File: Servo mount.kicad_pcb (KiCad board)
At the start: 2 copper layers, 80 x 34.6 mm, 35 parts, among them IC1 ATTINY84-SS, K5 CONN_3, K6 CONN_3, P1 CONN_3X2, Q1 BC847, Q2 BC847, U1 UA78L05, U2 BUZ11

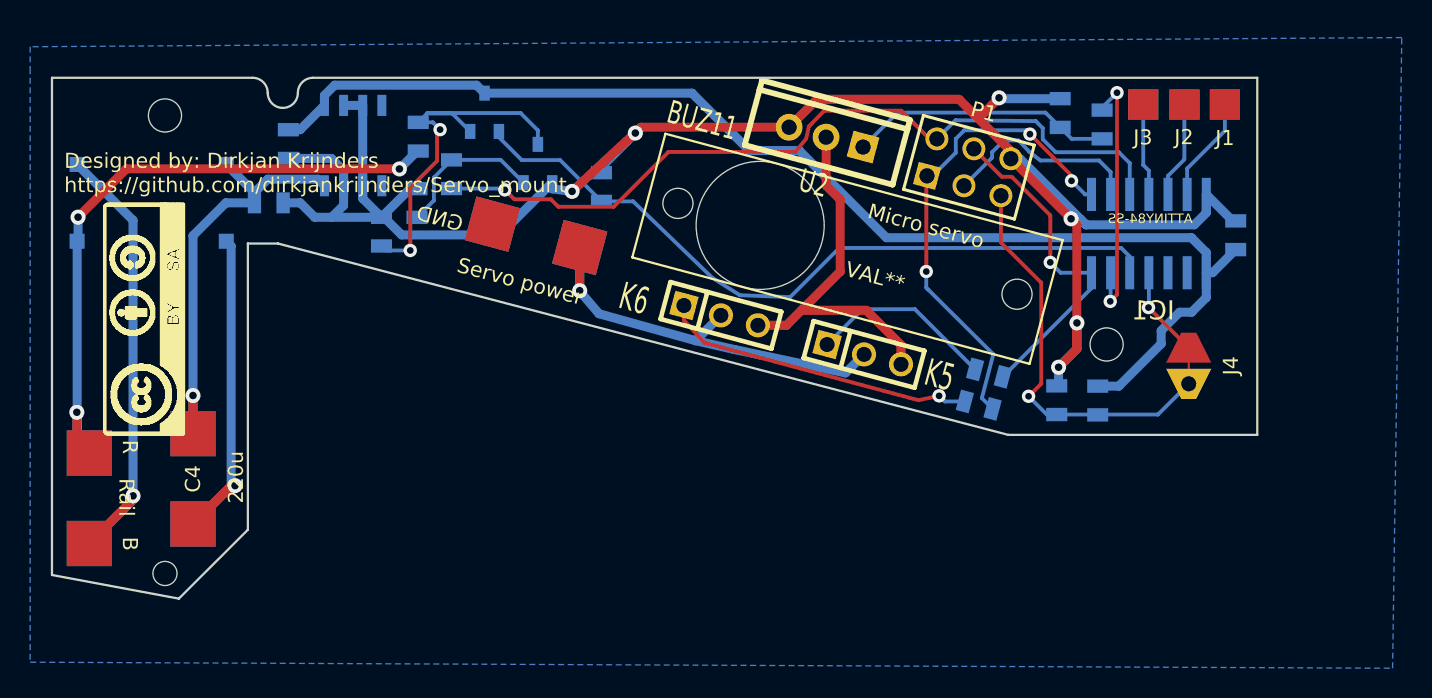
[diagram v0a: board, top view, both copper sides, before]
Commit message: Fixed rev 1 issues
- Moved all pad away from foot to allow for mounting under crossing
- Fixed the “hole” for the servo
- Fixed the order of J4 to really allow debug wire access
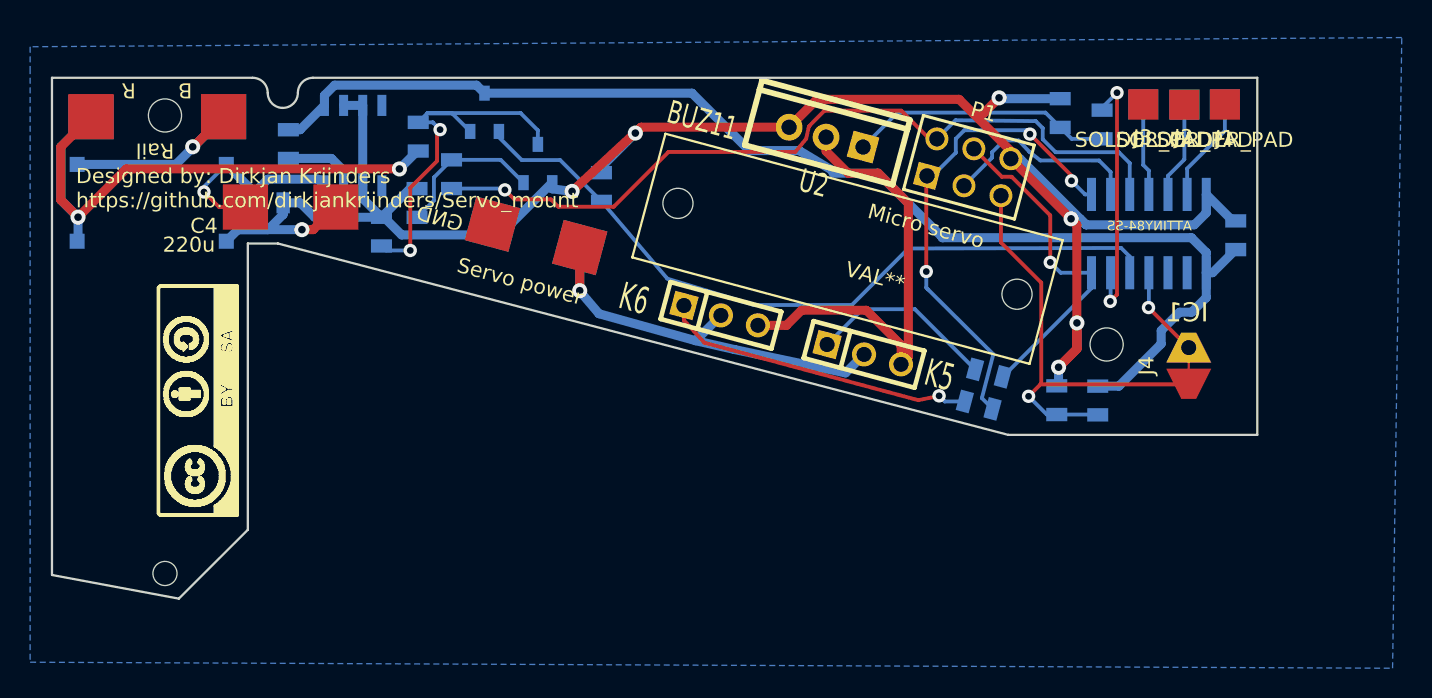
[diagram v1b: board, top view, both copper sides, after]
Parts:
- J1, J2, J3: value ~ -> SOLDER_PAD
- U1: value UA78L05 -> uA78L05
- moved ~ 25.5 mm to (105.6, 102.6), turned to 180 degrees
- moved C4 19.2 mm to (115.8, 108.6), turned to 0 degrees
- moved ? 6.48 mm to (112.3, 129.1)
- turned J4 to 90 degrees
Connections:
- IC1 pad 2: (no net) -> Net-(IC1-Pad2)
- IC1 pad 3: (no net) -> Net-(IC1-Pad3)
- IC1 pad 4: N-000009 -> Net-(IC1-Pad4)
- J4 pad 1: N-000009 -> Reset
- J4 pad 2: Reset -> Net-(IC1-Pad4)
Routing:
- net -VAA: track 32.3 -> 14.0 mm
- net Net-(C4-Pad1): track 32.4 -> 14.8 mm
- net GND: track 158.4 -> 143.2 mm
- net Net-(IC1-Pad4): track 0.00 -> 6.09 mm, vias 0 -> 1
- net N-000009: track 6.09 -> 0.00 mm, vias 1 -> 0
- net AGND: track 25.1 -> 30.9 mm
- net VAA: track 46.5 -> 42.0 mm, vias 3 -> 2
- net Reset: track 26.8 -> 29.7 mm

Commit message: Moved tracks away from servo hole
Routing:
- net AGND: track 30.9 -> 33.6 mm
- net Net-(K5-Pad1): track 12.4 -> 11.2 mm
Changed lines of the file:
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@@
     (thickness 1.6)
     (drawings 25)
-    (tracks 304)
+    (tracks 303)
     (zones 0)
     (modules 35)
@@
       (effects (font (size 1 1) (thickness 0.15)))
     )
-    (fp_circle (center -2 0) (end 0 -0.2) (layer Eco2.User) (width 2))
-    (fp_circle (center -6 0) (end -3.5 2) (layer Eco2.User) (width 2))
+    (fp_circle (center -2 0) (end 0 -0.2) (layer Edge.Cuts) (width 2))
+    (fp_circle (center -6 0) (end -3.5 2) (layer Edge.Cuts) (width 2))
     (fp_line (start 13.65 4.25) (end -13.65 4.25) (layer F.SilkS) (width 0.15))
     (fp_line (start -13.65 -4.25) (end 13.65 -4.25) (layer F.SilkS) (width 0.15))
@@
   (segment (start 108.22016 105.74984) (end 109.34 104.63) (width 0.6) (layer B.Cu) (net 2))
   (segment (start 109.34 104.63) (end 111.39 102.58) (width 0.6) (layer B.Cu) (net 2))
-  (segment (start 156.353452 119.0174) (end 156.84 118.530852) (width 0.6) (layer F.Cu) (net 3))
+  (segment (start 156.353452 119.0174) (end 160.09 115.280852) (width 0.6) (layer F.Cu) (net 3) (status 400000))
+  (segment (start 160.09 111.58) (end 154.84 106.33) (width 0.6) (layer F.Cu) (net 3))
+  (segment (start 160.09 115.280852) (end 160.09 111.58) (width 0.6) (layer F.Cu) (net 3))
+  (segment (start 154.84 106.33) (end 152.84 106.33) (width 0.6) (layer F.Cu) (net 3))
   (segment (start 151.38 104.87) (end 151.38 103.94) (width 0.6) (layer F.Cu) (net 3))
   (segment (start 152.84 106.33) (end 151.38 104.87) (width 0.6) (layer F.Cu) (net 3))
-  (segment (start 154.84 106.33) (end 152.84 106.33) (width 0.6) (layer F.Cu) (net 3))
-  (segment (start 156.84 108.33) (end 154.84 106.33) (width 0.6) (layer F.Cu) (net 3))
-  (segment (start 156.84 109.08) (end 156.84 108.33) (width 0.6) (layer F.Cu) (net 3))
-  (segment (start 156.84 118.530852) (end 156.84 109.08) (width 0.6) (layer F.Cu) (net 3))
   (segment (start 156.353452 119.0174) (end 156.353452 117.733452) (width 0.6) (layer F.Cu) (net 3))
   (segment (start 154.05 115.43) (end 149.75 115.43) (width 0.6) (layer F.Cu) (net 3))
@@
   (via (at 170.24 114.84) (size 0.889) (layers F.Cu B.Cu) (net 6))
   (segment (start 170.265 114.815) (end 170.24 114.84) (width 0.254) (layer B.Cu) (net 6))
+  (segment (start 162.34 117.58) (end 162.48 117.72) (width 0.254) (layer B.Cu) (net 7))
+  (segment (start 162.430044 121.976525) (end 161.72 121.26) (width 0.254) (layer B.Cu) (net 7))
+  (segment (start 161.72 121.26) (end 162.48 118.35) (width 0.254) (layer B.Cu) (net 7))
+  (segment (start 162.34 110.771477) (end 162.34 117.58) (width 0.254) (layer F.Cu) (net 7))
+  (via (at 162.34 117.58) (size 0.889) (layers F.Cu B.Cu) (net 7))
+  (segment (start 162.34 110.771477) (end 158.077848 106.509325) (width 0.254) (layer F.Cu) (net 7) (status 800000))
+  (segment (start 162.48 117.72) (end 162.48 118.35) (width 0.254) (layer B.Cu) (net 7))
   (segment (start 158.077848 106.509325) (end 158.450675 106.509325) (width 0.254) (layer B.Cu) (net 7))
   (via (at 167.67 106.84) (size 0.889) (layers F.Cu B.Cu) (net 7))
@@
   (segment (start 158.450675 106.509325) (end 159.99 104.97) (width 0.254) (layer B.Cu) (net 7))
   (segment (start 158.077848 106.509325) (end 158.03 106.557173) (width 0.254) (layer F.Cu) (net 7))
-  (segment (start 161.72 121.26) (end 162.48 118.35) (width 0.254) (layer B.Cu) (net 7))
-  (segment (start 162.48 118.35) (end 158.15 114.05) (width 0.254) (layer B.Cu) (net 7))
-  (segment (start 161.72 121.26) (end 162.430044 121.976525) (width 0.254) (layer B.Cu) (net 7))
-  (segment (start 158.03 113.93) (end 158.15 114.05) (width 0.254) (layer B.Cu) (net 7))
-  (segment (start 158.03 112.86) (end 158.03 113.93) (width 0.254) (layer B.Cu) (net 7))
-  (via (at 158.03 112.86) (size 0.889) (layers F.Cu B.Cu) (net 7))
-  (segment (start 158.03 106.557173) (end 158.03 112.86) (width 0.254) (layer F.Cu) (net 7))
   (segment (start 168.995 112.93842) (end 166.94842 112.93842) (width 0.254) (layer B.Cu) (net 8))
   (segment (start 163.045426 106.57) (end 161.1887 104.713274) (width 0.254) (layer F.Cu) (net 8))
@@
   (segment (start 175.44 117.91) (end 175.45 117.91) (width 0.254) (layer F.Cu) (net 16))
   (segment (start 172.78 115.25) (end 175.44 117.91) (width 0.254) (layer F.Cu) (net 16))
-  (segment (start 161.269956 119.353475) (end 157.276481 115.36) (width 0.254) (layer B.Cu) (net 17))
-  (segment (start 153.789148 115.36) (end 151.446548 117.7026) (width 0.254) (layer B.Cu) (net 17))
-  (segment (start 157.276481 115.36) (end 153.789148 115.36) (width 0.254) (layer B.Cu) (net 17))
+  (segment (start 161.269956 119.353475) (end 158.746481 116.83) (width 0.254) (layer B.Cu) (net 17) (status 400000))
+  (segment (start 152.319148 116.83) (end 151.446548 117.7026) (width 0.254) (layer B.Cu) (net 17) (status 800000))
+  (segment (start 158.746481 116.83) (end 152.319148 116.83) (width 0.254) (layer B.Cu) (net 17))
   (segment (start 141.946548 115.1126) (end 141.946548 116.096548) (width 0.254) (layer F.Cu) (net 18))
   (segment (start 159.253475 121.483475) (end 160.589956 121.483475) (width 0.254) (layer B.Cu) (net 18))
@@
   (segment (start 146.59 115.08) (end 140.84 113.33) (width 0.254) (layer B.Cu) (net 21))
   (segment (start 140.84 113.33) (end 136.59 108.33) (width 0.254) (layer B.Cu) (net 21))
-  (segment (start 153.09 115.08) (end 146.59 115.08) (width 0.254) (layer B.Cu) (net 21))
-  (segment (start 156.84 111.33) (end 153.09 115.08) (width 0.254) (layer B.Cu) (net 21))
-  (segment (start 170.965004 111.295004) (end 156.84 111.33) (width 0.254) (layer B.Cu) (net 21))
+  (segment (start 160.84 115.08) (end 146.59 115.08) (width 0.254) (layer B.Cu) (net 21))
+  (segment (start 164.609249 111.310751) (end 160.84 115.08) (width 0.254) (layer B.Cu) (net 21))
+  (segment (start 170.965004 111.295004) (end 164.609249 111.310751) (width 0.254) (layer B.Cu) (net 21))
   (segment (start 171.535 111.865) (end 170.965004 111.295004) (width 0.254) (layer B.Cu) (net 21))
   (segment (start 165.61 120.35) (end 175.41 120.35) (width 0.254) (layer F.Cu) (net 22))

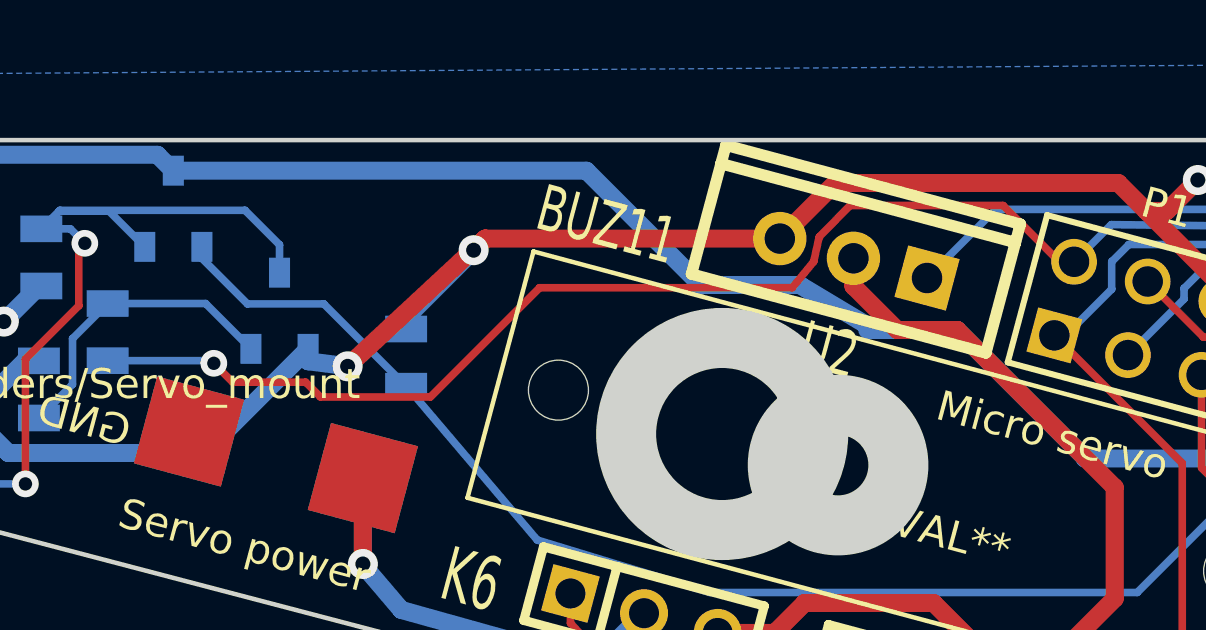
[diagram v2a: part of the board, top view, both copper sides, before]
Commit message: Fixed GND connection servo, fixed TO220 footprint
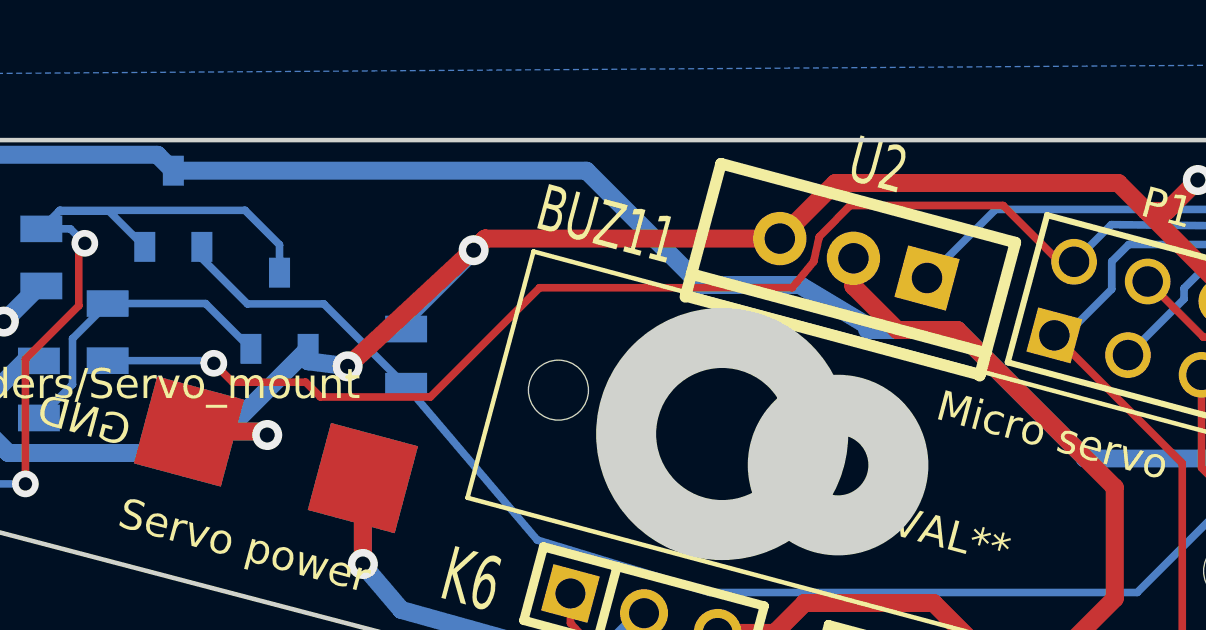
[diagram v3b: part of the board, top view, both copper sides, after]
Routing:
- net GND: track 143.2 -> 148.5 mm, vias 7 -> 8
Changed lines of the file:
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@@
   (general
     (links 66)
-    (no_connects 1)
+    (no_connects 0)
     (area 77.731 96.871 189.590001 139.190001)
     (thickness 1.6)
     (drawings 25)
-    (tracks 303)
+    (tracks 308)
     (zones 0)
     (modules 35)
@@
     (add_net VCC)
   )
+  (module TO220_VERT (layer F.Cu)
+    (at 151.38 103.94 75)
+    (descr "Regulateur TO220 serie LM78xx")
+    (tags "TR TO220")
+    (fp_text reference U2 (at 3.2 0 165) (layer F.SilkS)
+      (effects (font (size 1.524 1.016) (thickness 0.2032)))
+    )
+    (fp_text value BUZ11 (at -1.055315 -8.227199 165) (layer F.SilkS)
+      (effects (font (size 1.524 1.016) (thickness 0.2032)))
+    )
+    (fp_line (start -2.695 -5.08) (end -2.06 -5.08) (layer F.SilkS) (width 0.381))
+    (fp_line (start -2.66 -5.08) (end -2.66 5.08) (layer F.SilkS) (width 0.381))
+    (fp_line (start -2.06 5.08) (end -2.695 5.08) (layer F.SilkS) (width 0.381))
+    (fp_line (start -1.905 -5.08) (end 1.905 -5.08) (layer F.SilkS) (width 0.381))
+    (fp_line (start 1.905 -5.08) (end 1.905 5.08) (layer F.SilkS) (width 0.381))
+    (fp_line (start 1.905 5.08) (end -1.905 5.08) (layer F.SilkS) (width 0.381))
+    (fp_line (start -1.905 5.08) (end -1.905 -5.08) (layer F.SilkS) (width 0.381))
+    (pad S thru_hole circle (at 0 -2.54 75) (size 1.778 1.778) (drill 1.016) (layers *.Cu *.Mask F.SilkS)
+      (net 5 GND))
+    (pad D thru_hole circle (at 0 0 75) (size 1.778 1.778) (drill 1.016) (layers *.Cu *.Mask F.SilkS)
+      (net 3 AGND))
+    (pad G thru_hole rect (at 0 2.54 75) (size 1.778 1.778) (drill 1.016) (layers *.Cu *.Mask F.SilkS)
+      (net 20 "Net-(R2-Pad2)"))
+    (model Transistor_TO-220_Wings3d_RevB_03Sep2012/TO220-vert_RevB_Faktor03937_03Sep2012.wrl
+      (at (xyz 0 0 0))
+      (scale (xyz 0.4 0.4 0.4))
+      (rotate (xyz 0 0 270))
+    )
+  )
   (module Solderpad_2 (layer F.Cu)
     (at 115.84 108.58)
@@
       (net 5 GND))
   )
-  (module TO220_VERT (layer F.Cu)
-    (at 151.38 103.94 75)
-    (descr "Regulateur TO220 serie LM78xx")
-    (tags "TR TO220")
-    (fp_text reference U2 (at -3.175 0 165) (layer F.SilkS)
-      (effects (font (size 1.524 1.016) (thickness 0.2032)))
-    )
-    (fp_text value BUZ11 (at -1.055315 -8.227199 165) (layer F.SilkS)
-      (effects (font (size 1.524 1.016) (thickness 0.2032)))
-    )
-    (fp_line (start 1.905 -5.08) (end 2.54 -5.08) (layer F.SilkS) (width 0.381))
-    (fp_line (start 2.54 -5.08) (end 2.54 5.08) (layer F.SilkS) (width 0.381))
-    (fp_line (start 2.54 5.08) (end 1.905 5.08) (layer F.SilkS) (width 0.381))
-    (fp_line (start -1.905 -5.08) (end 1.905 -5.08) (layer F.SilkS) (width 0.381))
-    (fp_line (start 1.905 -5.08) (end 1.905 5.08) (layer F.SilkS) (width 0.381))
-    (fp_line (start 1.905 5.08) (end -1.905 5.08) (layer F.SilkS) (width 0.381))
-    (fp_line (start -1.905 5.08) (end -1.905 -5.08) (layer F.SilkS) (width 0.381))
-    (pad S thru_hole circle (at 0 -2.54 75) (size 1.778 1.778) (drill 1.016) (layers *.Cu *.Mask F.SilkS)
-      (net 5 GND))
-    (pad D thru_hole circle (at 0 0 75) (size 1.778 1.778) (drill 1.016) (layers *.Cu *.Mask F.SilkS)
-      (net 3 AGND))
-    (pad G thru_hole rect (at 0 2.54 75) (size 1.778 1.778) (drill 1.016) (layers *.Cu *.Mask F.SilkS)
-      (net 20 "Net-(R2-Pad2)"))
-  )
   (module M2 (layer F.Cu)
     (at 107.5 102.5)
@@
   (segment (start 108.22016 105.74984) (end 109.34 104.63) (width 0.6) (layer B.Cu) (net 2))
   (segment (start 109.34 104.63) (end 111.39 102.58) (width 0.6) (layer B.Cu) (net 2))
-  (segment (start 156.353452 119.0174) (end 160.09 115.280852) (width 0.6) (layer F.Cu) (net 3) (status 400000))
+  (segment (start 156.353452 119.0174) (end 160.09 115.280852) (width 0.6) (layer F.Cu) (net 3))
   (segment (start 160.09 111.58) (end 154.84 106.33) (width 0.6) (layer F.Cu) (net 3))
   (segment (start 160.09 115.280852) (end 160.09 111.58) (width 0.6) (layer F.Cu) (net 3))
@@
   (segment (start 165.76 104.08) (end 166.62 104.94) (width 0.254) (layer B.Cu) (net 4))
   (segment (start 159.973121 102.818002) (end 165.294877 102.87495) (width 0.254) (layer B.Cu) (net 4))
+  (segment (start 129.232223 109.713543) (end 131.723543 109.713543) (width 0.6) (layer F.Cu) (net 5) (status 400000))
+  (segment (start 131.723543 109.713543) (end 129.232223 109.713543) (width 0.6) (layer B.Cu) (net 5) (status 800000))
+  (segment (start 131.84 109.83) (end 131.723543 109.713543) (width 0.6) (layer B.Cu) (net 5))
+  (via (at 131.84 109.83) (size 1) (layers F.Cu B.Cu) (net 5))
+  (segment (start 131.723543 109.713543) (end 131.84 109.83) (width 0.6) (layer F.Cu) (net 5))
   (segment (start 111.57 110.85) (end 112.34 110.08) (width 0.6) (layer B.Cu) (net 5))
   (segment (start 112.34 110.08) (end 116.59 110.08) (width 0.6) (layer B.Cu) (net 5))
@@
   (segment (start 162.34 110.771477) (end 162.34 117.58) (width 0.254) (layer F.Cu) (net 7))
   (via (at 162.34 117.58) (size 0.889) (layers F.Cu B.Cu) (net 7))
-  (segment (start 162.34 110.771477) (end 158.077848 106.509325) (width 0.254) (layer F.Cu) (net 7) (status 800000))
+  (segment (start 162.34 110.771477) (end 158.077848 106.509325) (width 0.254) (layer F.Cu) (net 7))
   (segment (start 162.48 117.72) (end 162.48 118.35) (width 0.254) (layer B.Cu) (net 7))
   (segment (start 158.077848 106.509325) (end 158.450675 106.509325) (width 0.254) (layer B.Cu) (net 7))
@@
   (segment (start 175.44 117.91) (end 175.45 117.91) (width 0.254) (layer F.Cu) (net 16))
   (segment (start 172.78 115.25) (end 175.44 117.91) (width 0.254) (layer F.Cu) (net 16))
-  (segment (start 161.269956 119.353475) (end 158.746481 116.83) (width 0.254) (layer B.Cu) (net 17) (status 400000))
-  (segment (start 152.319148 116.83) (end 151.446548 117.7026) (width 0.254) (layer B.Cu) (net 17) (status 800000))
+  (segment (start 161.269956 119.353475) (end 158.746481 116.83) (width 0.254) (layer B.Cu) (net 17))
+  (segment (start 152.319148 116.83) (end 151.446548 117.7026) (width 0.254) (layer B.Cu) (net 17))
   (segment (start 158.746481 116.83) (end 152.319148 116.83) (width 0.254) (layer B.Cu) (net 17))
   (segment (start 141.946548 115.1126) (end 141.946548 116.096548) (width 0.254) (layer F.Cu) (net 18))
